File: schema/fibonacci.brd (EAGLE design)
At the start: 88.9 x 59.7 mm, 29 parts, among them IC1 DS1307, J1 POWER_JACK

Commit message: Board schema and layout v0.9
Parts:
- removed C6: 100nF, resistor:C050-025X075
- removed U$1: RPI_SD_HOLDER, xose:RPI1_SD_HOLDER
- added C3: 100nF, xose:C050-025X075
- added U$2: MicroSD, xose:DM3D
- 16MHZ: value (none) -> 16MHz; device special:QS -> xose:QS
- BATT: device adafruit:CR2032-SMD -> xose:CR2032-SMD
- BUTTON1: value TACTILE_BUTTON -> B1
- BUTTON2: value TACTILE_BUTTON -> B2
- BUTTON3: value TACTILE_BUTTON -> B3
- BUTTON4: value TACTILE_BUTTON -> B4
- C1, C2, C4, C5: device rcl:C025-025X050 -> xose:C050-025X075
- CRYSTAL: device adafruit:TC38H -> xose:TC38H
- IC1: device adafruit:DIL08 -> xose:DIL08
- J1: value POWER_JACK -> (none); device SparkFun-Connectors:POWER_JACK_PTH -> xose:POWER_JACK_PTH
- LED_TERMINAL: value (none) -> M03-SCREW-2.5MM; device SparkFun-Connectors:SCREWTERMINAL-5MM-3 -> xose:1X03_2.54_SCREWTERM
- MUC: device SparkFun-DigitalIC:DIL28-3 -> xose:DIL28-3
- POWER_TERMINAL: value (none) -> M02-SCREW-2.5MM; device SparkFun-Connectors:SCREWTERMINAL-5MM-2 -> xose:1X02_2.54_SCREWTERM
- R1, R2, R3, R4, R5, R6, R7, R8: device SparkFun-Resistors:AXIAL-0.4 -> xose:AXIAL-0.4
- R9: value 10K -> 1K8; device SparkFun-Resistors:AXIAL-0.4 -> xose:AXIAL-0.4
- REGULATOR: value (none) -> TSC295033; device national-semiconductor:TO92 -> xose:TO92
- moved LED_TERMINAL 84.1 mm to (85.1, 48.9)
- moved POWER_TERMINAL 19.9 mm to (3.81, 40.0), flipped to the top, turned to 90 degrees
- moved C1 17.3 mm to (17.1, 4.45)
- moved J1 13.4 mm to (-3.17, 31.1)
- moved REGULATOR 12.2 mm to (11.4, 4.45), flipped to the bottom, turned to 270 degrees
- moved BATT 8.98 mm to (34.3, 10.2), flipped to the top
- moved R6 3.17 mm to (17.1, 30.5)
- moved R5 2.54 mm to (21.6, 30.5)
- moved R4 1.91 mm to (26.0, 30.5)
- moved BUTTON2 1.27 mm to (57.1, 50.8)
- moved BUTTON3 1.27 mm to (43.2, 50.8)
- moved BUTTON4 1.27 mm to (29.2, 50.8)
- moved MUC 1.27 mm to (62.2, 21.6)
- moved R3 1.27 mm to (30.5, 30.5)
- moved BUTTON1 1.27 mm to (71.1, 50.8)
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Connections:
- new net N$14: U$2.GND1
- new net N$15: U$2.GND2
- new net N$16: U$2.GND3
- new net N$17: U$2.GND4
- net 3V3: now also U$2.VDD; no longer U$1.4
- net 5V: now also LED_TERMINAL.P3, POWER_TERMINAL.P1, R9.P$2; no longer LED_TERMINAL.3, POWER_TERMINAL.2, R9.P$1
- net DATA: now also LED_TERMINAL.P2, MUC.6; no longer LED_TERMINAL.2, MUC.15
- net DTR: now also C3.2; no longer C6.1
- net GND: now also C4.2, C5.2, LED_TERMINAL.P1, POWER_TERMINAL.P2, U$2.CMD, U$2.VSS; no longer C4.1, C5.1, LED_TERMINAL.1, POWER_TERMINAL.1, U$1.3, U$1.6
- net MISO: now also U$2.DAT0; no longer U$1.7
- net N$1: now also C3.1, R9.P$1; no longer C6.2, R9.P$2
- net N$2: now also C4.1; no longer C4.2
- net N$3: now also C5.1; no longer C5.2
- net N$4: now also BATT.+$1; no longer BATT.+$2
- net SD_MOSI: now also U$2.CD/DAT3; no longer U$1.2
- net SD_SCK: now also U$2.CLK; no longer U$1.5
- net SD_SS: now also U$2.DAT2; no longer U$1.1
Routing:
- net SD_SS: track 10.4 -> 45.9 mm
- net GND: track 320.8 -> 291.0 mm, vias 2 -> 3
- net SD_MOSI: track 11.2 -> 36.5 mm
- net 3V3: track 50.4 -> 28.8 mm, vias 0 -> 2
- net DATA: track 51.0 -> 30.7 mm, vias 2 -> 0
- net SD_SCK: track 13.4 -> 27.4 mm
- net MISO: track 40.2 -> 53.5 mm, vias 1 -> 2
- net 5V: track 207.4 -> 220.0 mm, vias 0 -> 1
- net N$4: track 23.4 -> 12.7 mm
- net N$5: track 3.81 -> 6.88 mm
- net RXD: track 14.3 -> 11.3 mm
- net BUTTON4: track 34.2 -> 36.7 mm
- net BUTTON3: track 22.8 -> 25.2 mm
- net TXD: track 22.6 -> 21.3 mm, vias 1 -> 0
- net SDA: track 26.2 -> 25.0 mm
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- added copper zone on layer 16, net GND
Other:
- outline, holes or cut-outs redrawn
- board text added: "5V"
- board text added: "DACLOCK"
- board text added: "DATA"
- board text added: "GND"
- board text added: "Tinkerman 2015"

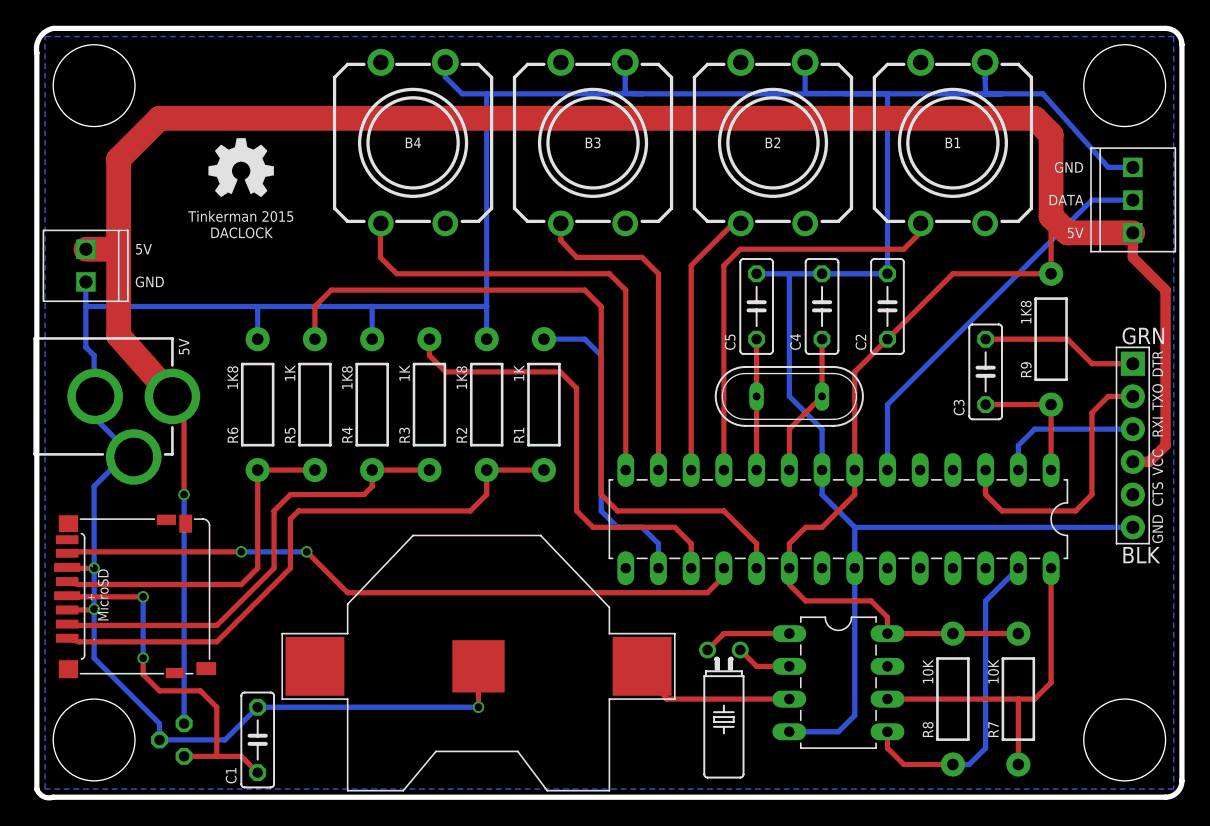
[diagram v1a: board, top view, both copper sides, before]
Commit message: Added beefier terminals to board
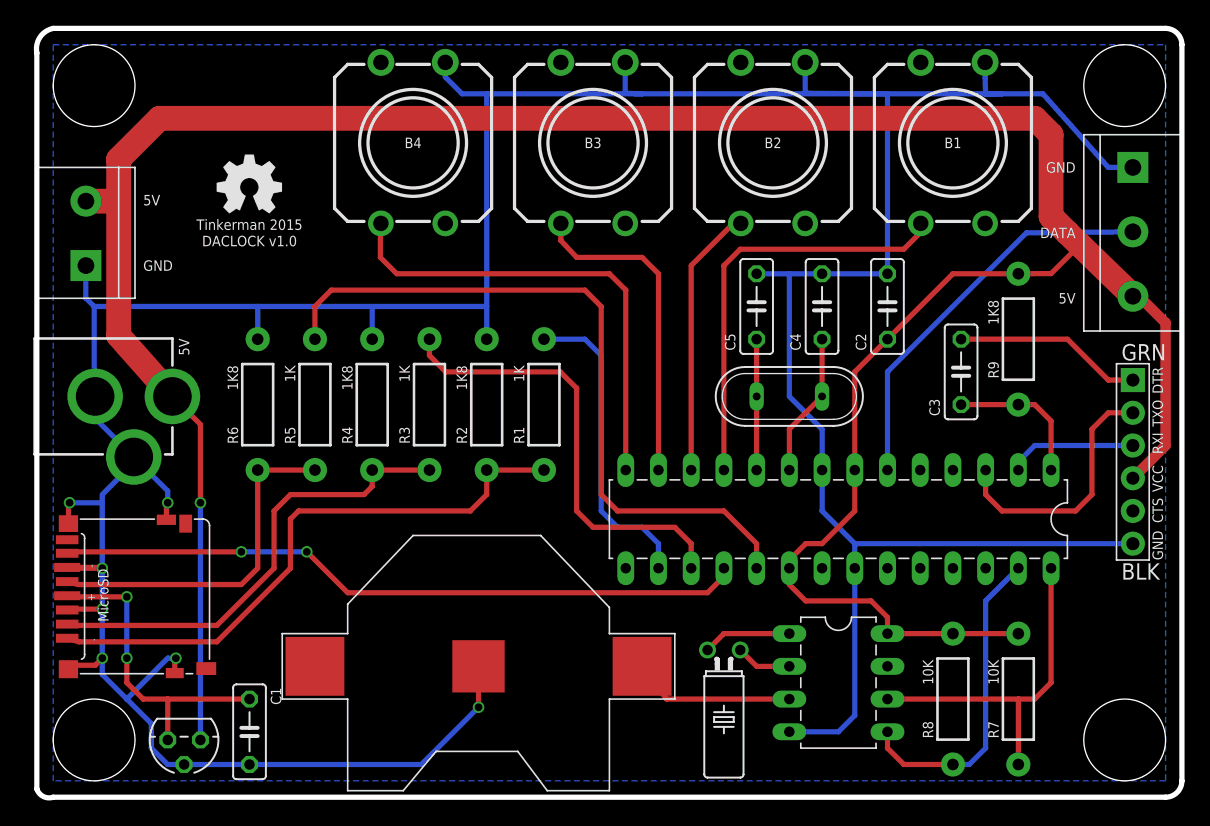
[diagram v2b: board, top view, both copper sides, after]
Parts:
- LED_TERMINAL: value M03-SCREW-2.5MM -> M03-SCREW-200MIL; device xose:1X03_2.54_SCREWTERM -> xose:SCREWTERMINAL-200MIL-3
- POWER_TERMINAL: value M02-SCREW-2.5MM -> M02-SCREW-200MIL; device xose:1X02_2.54_SCREWTERM -> xose:SCREWTERMINAL-200MIL-2
- moved R9 2.54 mm to (76.2, 35.6)
- moved C3 1.91 mm to (71.8, 33.0)
- moved JP1 1.27 mm to (85.1, 26.0)
- moved POWER_TERMINAL 1.27 mm to (3.81, 41.3)
- moved C1 0.90 mm to (16.5, 5.08), turned to 270 degrees
- flipped REGULATOR to the top, turned to 180 degrees
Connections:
- removed net N$14: U$2.GND1
- removed net N$15: U$2.GND2
- removed net N$16: U$2.GND3
- removed net N$17: U$2.GND4
- net 5V: now also LED_TERMINAL.3, POWER_TERMINAL.2; no longer LED_TERMINAL.P3, POWER_TERMINAL.P1
- net DATA: now also LED_TERMINAL.2; no longer LED_TERMINAL.P2
- net GND: now also LED_TERMINAL.1, POWER_TERMINAL.1, U$2.GND1, U$2.GND2, U$2.GND3, U$2.GND4; no longer LED_TERMINAL.P1, POWER_TERMINAL.P2
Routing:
- net GND: track 291.0 -> 317.2 mm, vias 3 -> 7
- net 3V3: track 28.8 -> 24.6 mm
- net DTR: track 12.2 -> 14.7 mm
- net 5V: track 220.0 -> 218.5 mm
- net TXD: track 21.3 -> 20.0 mm
- net RXD: track 11.3 -> 10.1 mm
- net N$1: track 10.2 -> 11.3 mm
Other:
- board text added: "DACLOCK v1.0"
- board text removed: "DACLOCK"

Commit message: Final PCB version and gerbers
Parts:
- removed MUC: ATMEGA328P, xose:DIL28-3
- added IC2: DS1307, xose:DIL08
- IC1: value DS1307 -> ATMEGA328P; device xose:DIL08 -> xose:DIL28-3
- U$2: value MicroSD -> uSD
- moved IC1 12.7 mm to (62.2, 21.6), turned to 180 degrees
- renumbered 16MHZ to XTAL1, CRYSTAL to XTAL2, REGULATOR to LDO1
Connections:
- net 5V: now also IC1.20, IC1.7, IC2.8; no longer IC1.8, MUC.20, MUC.7
- net BUTTON1: now also IC1.11; no longer MUC.11
- net BUTTON2: now also IC1.12; no longer MUC.12
- net BUTTON3: now also IC1.13; no longer MUC.13
- net BUTTON4: now also IC1.14; no longer MUC.14
- net DATA: now also IC1.6; no longer MUC.6
- net GND: now also IC1.22, IC1.8, IC2.4; no longer IC1.4, MUC.22, MUC.8
- net MISO: now also IC1.18; no longer MUC.18
- net MOSI: now also IC1.17; no longer MUC.17
- net N$1: now also IC1.1; no longer MUC.1
- net N$2: now also IC1.9; no longer MUC.9
- net N$3: now also IC1.10; no longer MUC.10
- net N$4: now also IC2.3; no longer IC1.3
- net N$5: now also IC2.1; no longer IC1.1
- net N$6: now also IC2.2; no longer IC1.2
- net RXD: now also IC1.2; no longer MUC.2
- net SCK: now also IC1.19; no longer MUC.19
- net SCL: now also IC1.28, IC2.6; no longer IC1.6, MUC.28
- net SDA: now also IC1.27, IC2.5; no longer IC1.5, MUC.27
- net SS: now also IC1.16; no longer MUC.16
- net TXD: now also IC1.3; no longer MUC.3

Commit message: Schema and board layout, datasheets
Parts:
- moved LDO1 0.64 mm to (11.4, 3.81), turned to 0 degrees
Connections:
- net 3V3: now also LDO1.OUT; no longer LDO1.3
- net 5V: now also LDO1.IN; no longer LDO1.1
- net GND: now also LDO1.GND; no longer LDO1.2
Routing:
- net GND: track 317.2 -> 307.2 mm
- net 5V: track 218.5 -> 219.2 mm
- net 3V3: track 24.6 -> 25.2 mm
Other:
- outline, holes or cut-outs redrawn
- board text added: "Tinkerman 2015 DACLOCK v1.1"
- board text removed: "DACLOCK v1.0"
- board text removed: "Tinkerman 2015"
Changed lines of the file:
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@@
 <board>
 <plain>
-<circle x="4.445" y="55.245" radius="3.175" width="0.0254" layer="20"/>
+<circle x="4.445" y="55.245" radius="1.905" width="0.0254" layer="20"/>
 <wire x1="87.63" y1="0" x2="1.27" y2="0" width="0.4064" layer="20"/>
 <wire x1="1.27" y1="0" x2="0" y2="0.635" width="0.4064" layer="20" curve="-90"/>
@@
 <wire x1="88.9" y1="58.42" x2="88.9" y2="1.27" width="0.4064" layer="20"/>
 <wire x1="88.9" y1="1.27" x2="87.63" y2="0" width="0.4064" layer="20" curve="-90"/>
-<circle x="4.445" y="4.445" radius="3.175" width="0.0254" layer="20"/>
-<circle x="84.455" y="55.245" radius="3.175" width="0.0254" layer="20"/>
-<circle x="84.455" y="4.445" radius="3.175" width="0.0254" layer="20"/>
+<circle x="4.445" y="4.445" radius="1.905" width="0.0254" layer="20"/>
+<circle x="84.455" y="55.245" radius="1.905" width="0.0254" layer="20"/>
+<circle x="84.455" y="4.445" radius="1.905" width="0.0254" layer="20"/>
 <text x="8.255" y="46.355" size="0.8128" layer="21" font="vector" ratio="15" rot="R90" align="top-center">5V</text>
 <text x="8.255" y="41.275" size="0.8128" layer="21" font="vector" ratio="15" rot="R90" align="top-center">GND</text>
@@
 <rectangle x1="16.1417" y1="49.8475" x2="16.8529" y2="49.8729" layer="25"/>
 <rectangle x1="16.1417" y1="49.8729" x2="16.8529" y2="49.8983" layer="25"/>
-<text x="16.51" y="44.45" size="0.8128" layer="21" font="vector" ratio="15" align="center">Tinkerman 2015</text>
-<text x="16.51" y="43.18" size="0.8128" layer="21" font="vector" ratio="15" align="center">DACLOCK v1.0</text>
+<text x="16.51" y="43.815" size="0.8128" layer="21" font="vector" ratio="15" align="center">Tinkerman 2015
+DACLOCK v1.1</text>
 <text x="11.43" y="34.29" size="0.8128" layer="21" font="vector" ratio="15" rot="R90" align="center-left">5V</text>
 </plain>
@@
 </element>
 <element name="C3" library="xose" package="C050-025X075" value="100nF" x="71.755" y="33.02" rot="R90"/>
-<element name="LDO1" library="xose" package="TO92" value="TSC295033" x="11.43" y="4.445" rot="R180">
-<attribute name="MF" value="NATIONAL SEMICONDUCTOR" x="11.43" y="-3.175" size="1.778" layer="27" rot="R180" display="off"/>
-<attribute name="MPN" value="LP2950CZ-5.0/NOPB" x="11.43" y="-3.175" size="1.778" layer="27" rot="R180" display="off"/>
-<attribute name="OC_FARNELL" value="1150320" x="11.43" y="-3.175" size="1.778" layer="27" rot="R180" display="off"/>
-<attribute name="OC_NEWARK" value="41K6545" x="11.43" y="-3.175" size="1.778" layer="27" rot="R180" display="off"/>
+<element name="LDO1" library="xose" package="TO92" value="TSC295033" x="11.43" y="3.81">
+<attribute name="MF" value="NATIONAL SEMICONDUCTOR" x="11.43" y="11.43" size="1.778" layer="27" display="off"/>
+<attribute name="MPN" value="LP2950CZ-5.0/NOPB" x="11.43" y="11.43" size="1.778" layer="27" display="off"/>
+<attribute name="OC_FARNELL" value="1150320" x="11.43" y="11.43" size="1.778" layer="27" display="off"/>
+<attribute name="OC_NEWARK" value="41K6545" x="11.43" y="11.43" size="1.778" layer="27" display="off"/>
 </element>
 <element name="C1" library="xose" package="C050-025X075" value="330nF" x="16.51" y="5.08" rot="R270"/>
@@
 <contactref element="LED_TERMINAL" pad="1"/>
 <contactref element="BATT" pad="-"/>
-<contactref element="LDO1" pad="2"/>
+<contactref element="LDO1" pad="GND"/>
 <contactref element="C1" pad="2"/>
 <contactref element="R2" pad="P$2"/>
@@
 <wire x1="5.08" y1="9.525" x2="6.985" y2="7.62" width="0.4064" layer="16"/>
 <wire x1="6.985" y1="7.62" x2="8.89" y2="5.715" width="0.4064" layer="16"/>
-<wire x1="8.89" y1="5.715" x2="8.89" y2="3.81" width="0.4064" layer="16"/>
-<wire x1="8.89" y1="3.81" x2="10.16" y2="2.54" width="0.4064" layer="16"/>
-<wire x1="10.16" y1="2.54" x2="11.43" y2="2.54" width="0.4064" layer="16"/>
-<wire x1="11.43" y1="2.54" x2="16.51" y2="2.54" width="0.4064" layer="16"/>
 <wire x1="16.51" y1="2.54" x2="29.845" y2="2.54" width="0.4064" layer="16"/>
 <wire x1="29.845" y1="2.54" x2="34.29" y2="6.985" width="0.4064" layer="16"/>
@@
 <contactref element="IC1" pad="20"/>
 <contactref element="IC1" pad="7"/>
-<contactref element="LDO1" pad="1"/>
+<contactref element="LDO1" pad="IN"/>
 <contactref element="J1" pad="PWR"/>
 <contactref element="LED_TERMINAL" pad="3"/>
@@
 <wire x1="10.525" y1="31.115" x2="10.525" y2="30.75" width="0.4064" layer="1"/>
 <wire x1="10.525" y1="30.75" x2="10.795" y2="30.48" width="0.4064" layer="1"/>
-<wire x1="12.7" y1="4.445" x2="12.7" y2="22.86" width="0.4064" layer="16"/>
 <via x="12.7" y="22.86" extent="1-16" drill="0.6" shape="square"/>
 <wire x1="12.7" y1="22.86" x2="12.7" y2="28.94" width="0.4064" layer="1"/>
@@
 <wire x1="3.81" y1="46.275" x2="6.27" y2="46.275" width="1.9304" layer="1"/>
 <wire x1="6.27" y1="46.275" x2="6.35" y2="46.355" width="1.9304" layer="1"/>
+<wire x1="12.7" y1="22.86" x2="12.7" y2="3.81" width="0.4064" layer="16"/>
 </signal>
 <signal name="N$1">
@@
 </signal>
 <signal name="3V3">
-<contactref element="LDO1" pad="3"/>
+<contactref element="LDO1" pad="OUT"/>
 <contactref element="C1" pad="1"/>
 <contactref element="U$2" pad="VDD"/>
@@
 <wire x1="6.985" y1="15.5575" x2="2.4375" y2="15.5575" width="0.4064" layer="1"/>
 <wire x1="2.4375" y1="15.5575" x2="2.355" y2="15.64" width="0.4064" layer="1"/>
-<wire x1="10.16" y1="4.445" x2="10.16" y2="7.62" width="0.4064" layer="1"/>
+<wire x1="10.16" y1="3.81" x2="10.16" y2="7.62" width="0.4064" layer="1"/>
 <wire x1="16.51" y1="7.62" x2="10.16" y2="7.62" width="0.4064" layer="1"/>
 </signal>
@@
 </board>
 </drawing>
+<compatibility>
+<note version="6.3" minversion="6.2.2" severity="warning">
+Since Version 6.2.2 text objects can contain more than one line,
+which will not be processed correctly with this version.
+</note>
+</compatibility>
 </eagle>
